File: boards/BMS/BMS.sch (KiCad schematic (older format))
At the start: 30 parts

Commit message: began isoSPI sheet, continued main sheet
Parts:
- added C?: C_0.1uF, Capacitors_SMD:C_0805, symbol C_0.1uF
- added D? (x5): LED_0805, LEDs:LED_0805, symbol LED_0805
- added Q? (x2): NMOS_GSD_30V, TO_SOT_Packages_SMD:SOT-23, symbol NMOS_GSD_30V
- added R? (x2): R_100k, Resistors_SMD:R_0805, symbol R_100k
- added R? (x2): R_10k, Resistors_SMD:R_0805, symbol R_10k
- added R? (x2): 649, symbol R
- added R? (x3): R_200, Resistors_SMD:R_0805, symbol R_200
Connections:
- net BSPD_Current_Sense: now also IC?.23 ((PCINT3/AMP0-)PB3)
- net GND: now also U?.3 (GND), C?.2, Q?.2 (S), Q?.2 (S), R?.1, R?.1, R?.1, R?.1, R?.2, R?.2, R?.2
- net LED1: now also IC?.17 ((PCINT12/ADC8/ACMPN3/AMP1-)PC4)
- net LED2: now also IC?.18 ((PCINT13/ADC9/ACMP3/AMP1+)PC5)
- net VCC: now also U?.5 (VCC), C?.1, R?.1, R?.1
- net Sense_Shutdown_N: now reaches IC?.14 ((PCINT22/ADC3/INT0/ACMPN2)PD6)
- net Sense_Shutdown_N: now also Q?.3 (D), R?.2
- net Sense_Shutdown_S: now reaches IC?.15 ((PCINT23/ACMP0)PD7)
- net Sense_Shutdown_S: now also Q?.3 (D), R?.2
- net Shutdown_Control: now reaches IC?.16 ((PCINT2/ADC5/INT1/ACMPN0)PB2)
- net CS_iso: now reaches IC?.24 ((PCINT4/AMP0+)PB4)
- net LED3: now reaches IC?.26 ((PCINT5/ADC6/INT2/ACMPN1/AMP2-)PB5)
- net LED3: now also D?.2 (A)
- net LED4: now reaches IC?.27 ((PCINT6/ADC7/PSCOUT1B)PB6)
- net LED4: now also D?.2 (A)
- net SCK_iso: now reaches IC?.28 ((PCINT7/ADC4/SCK/PSCOUT0B)PB7)
- net Fan_PWM: now reaches IC?.3 ((PCINT9/PSCIN1/OC1B/~SS_A~)PC1)
- net LED5: now reaches IC?.30 ((PCINT8/INT3/PSCOUT1A)PC0)
- net LED5: now also D?.2 (A)
- net MISO_iso: now reaches IC?.8 ((PCINT0/MISO/PSCOUT2A)PB0)
- net MOSI_iso: now reaches IC?.9 ((PCINT1/MOSI/PSCOUT2B)PB1)
- new net: D?.1 (K), R?.2 (x2)
- new net: D?.1 (K), R?.1 (x3)
- new net Shutdown_N: D?.2 (A), Q?.1 (G), R?.2
- new net Shutdown_S: D?.2 (A), Q?.1 (G), R?.2
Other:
- moved on the sheet: R?

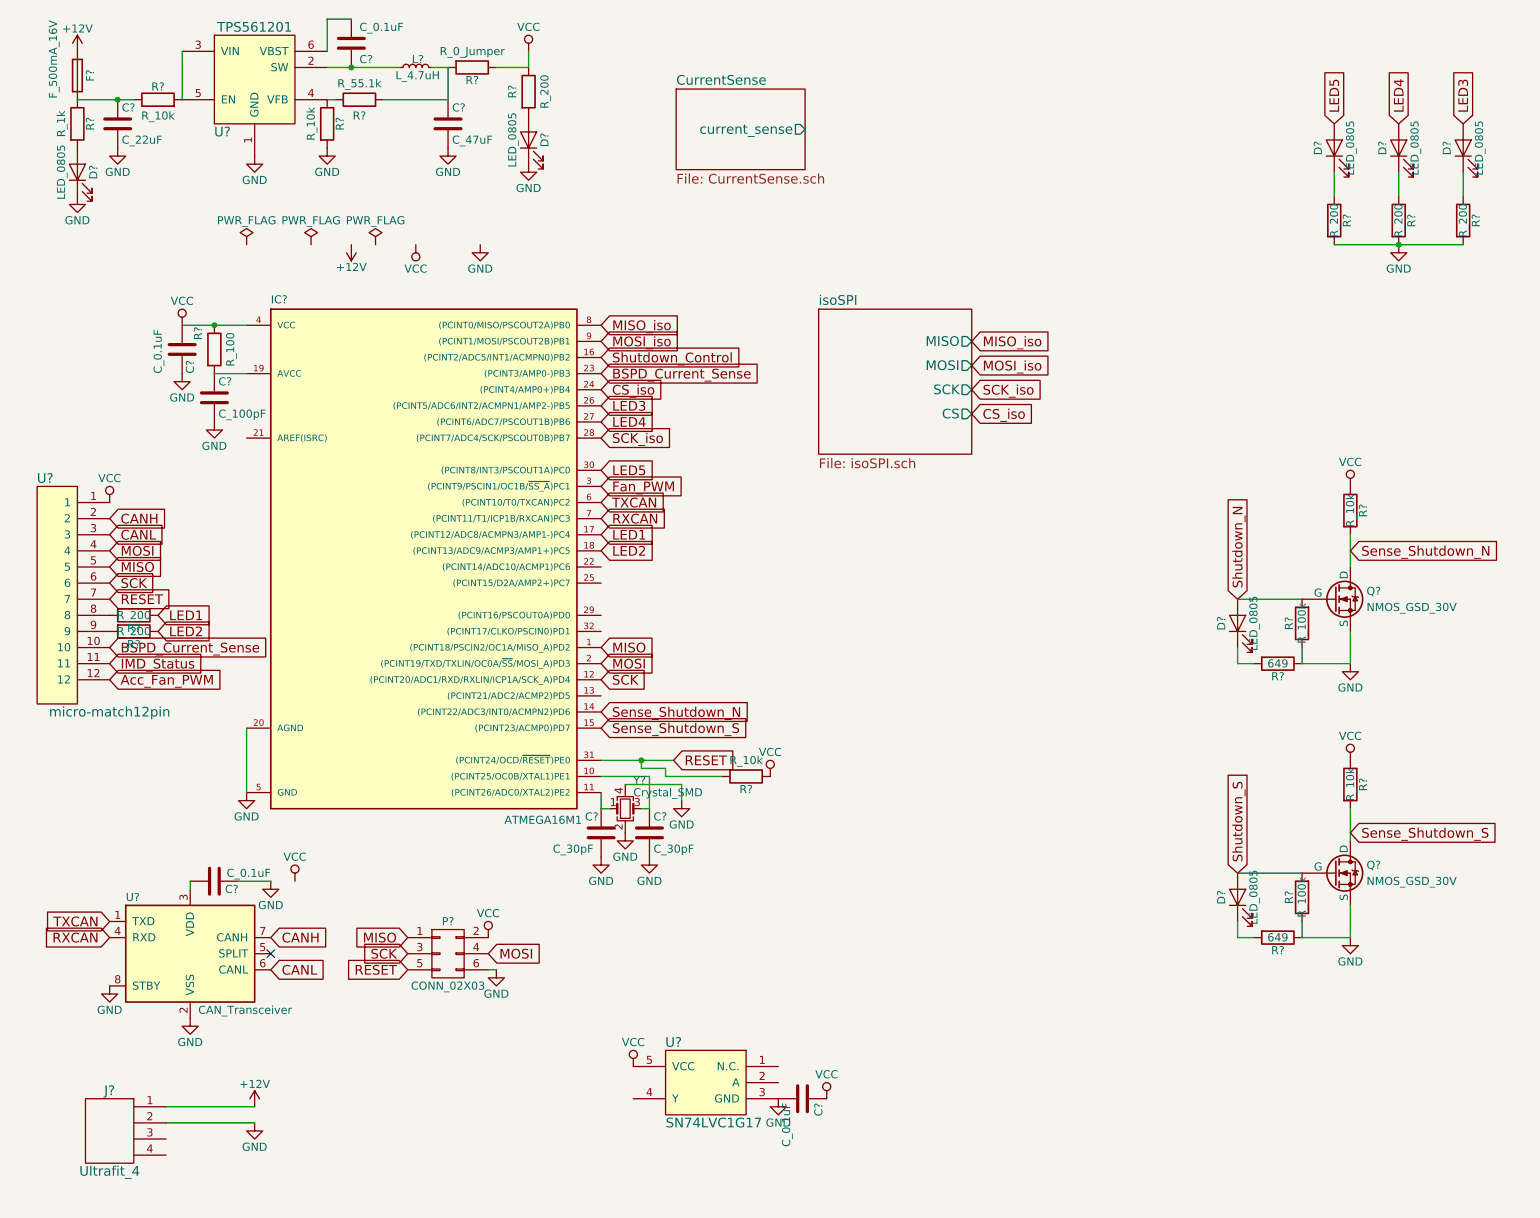
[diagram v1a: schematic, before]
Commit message: balance schematic for BMS slave
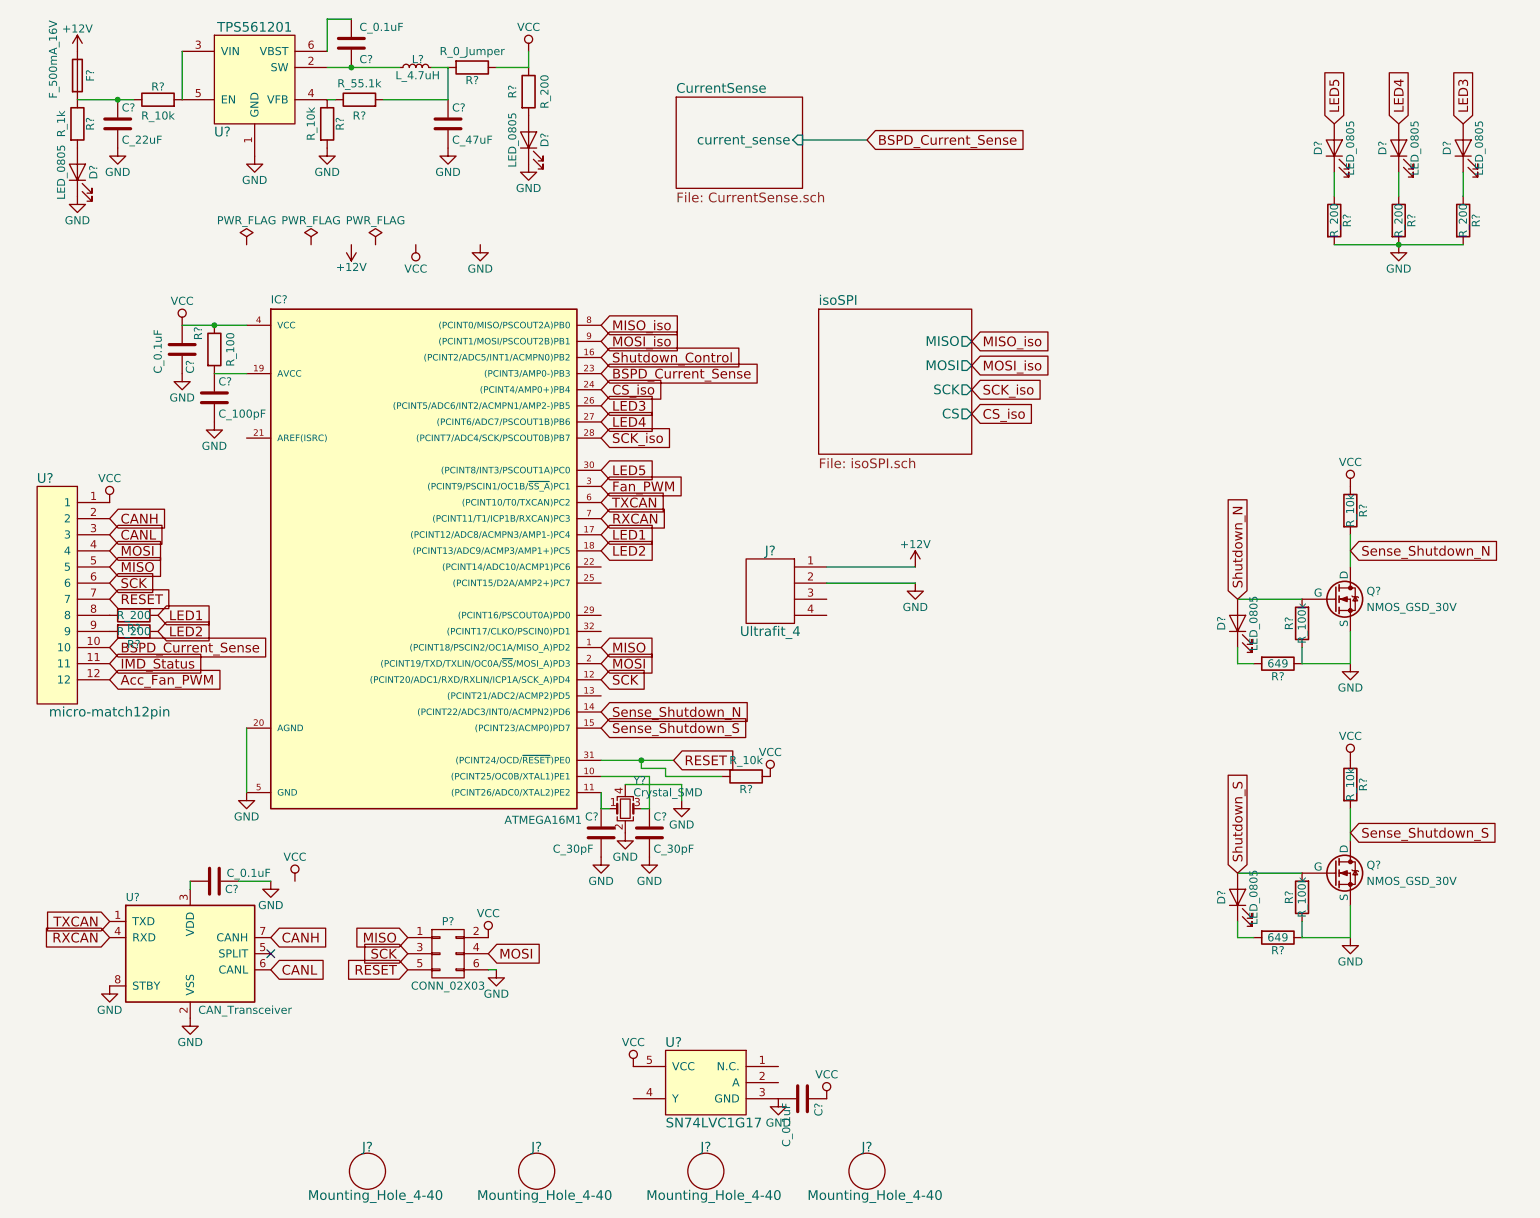
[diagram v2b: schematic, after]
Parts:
- added J? (x4): Mounting_Hole_4-40, footprints:Mounting_Hole_4-40, symbol Mounting_Hole_4-40
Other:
- moved on the sheet: J?
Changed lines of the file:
@@
 L Ultrafit_4 J?
 U 1 1 59E24F97
-P 1000 7600
-F 0 "J?" H 1000 7900 60  0000 C CNN
-F 1 "Ultrafit_4" H 1000 7400 60  0000 C CNN
-F 2 "footprints:Ultrafit_4" H 900 7850 60  0001 C CNN
-F 3 "http://www.literature.molex.com/SQLImages/kelmscott/Molex/PDF_Images/987651-1008.pdf" H 1000 7950 60  0001 C CNN
-F 4 "Digi-Key" H 1000 7600 60  0001 C CNN "MFN"
-F 5 "Value" H 1000 7600 60  0001 C CNN "Package"
-F 6 "WM11574-ND" H 1000 7600 60  0001 C CNN "MPN"
-F 7 "WM11564-ND" H 1400 8350 60  0001 C CNN "MPN2"
-F 8 "https://www.digikey.com/products/en?keywords=WM11574-ND" H 1500 8450 60  0001 C CNN "PurchasingLink"
-F 9 "https://www.digikey.com/product-detail/en/molex-llc/1722561004/WM11564-ND/5291228" H 1600 8550 60  0001 C CNN "PurchasingLink2"
-	1    1000 7600
+P 5100 4250
+F 0 "J?" H 5100 4550 60  0000 C CNN
+F 1 "Ultrafit_4" H 5100 4050 60  0000 C CNN
+F 2 "footprints:Ultrafit_4" H 5000 4500 60  0001 C CNN
+F 3 "http://www.literature.molex.com/SQLImages/kelmscott/Molex/PDF_Images/987651-1008.pdf" H 5100 4600 60  0001 C CNN
+F 4 "Digi-Key" H 5100 4250 60  0001 C CNN "MFN"
+F 5 "Value" H 5100 4250 60  0001 C CNN "Package"
+F 6 "WM11574-ND" H 5100 4250 60  0001 C CNN "MPN"
+F 7 "WM11564-ND" H 5500 5000 60  0001 C CNN "MPN2"
+F 8 "https://www.digikey.com/products/en?keywords=WM11574-ND" H 5600 5100 60  0001 C CNN "PurchasingLink"
+F 9 "https://www.digikey.com/product-detail/en/molex-llc/1722561004/WM11564-ND/5291228" H 5700 5200 60  0001 C CNN "PurchasingLink2"
+	1    5100 4250
 	1    0    0    -1
 $EndComp
@@
 L GND #PWR?
 U 1 1 59E25104
-P 1900 7500
-F 0 "#PWR?" H 1900 7250 50  0001 C CNN
-F 1 "GND" H 1900 7350 50  0000 C CNN
-F 2 "" H 1900 7500 50  0001 C CNN
-F 3 "" H 1900 7500 50  0001 C CNN
-	1    1900 7500
-	1    0    0    -1
-$EndComp
-Wire Wire Line
-	1350 7500 1900 7500
+P 6000 4150
+F 0 "#PWR?" H 6000 3900 50  0001 C CNN
+F 1 "GND" H 6000 4000 50  0000 C CNN
+F 2 "" H 6000 4150 50  0001 C CNN
+F 3 "" H 6000 4150 50  0001 C CNN
+	1    6000 4150
+	1    0    0    -1
+$EndComp
+Wire Wire Line
+	5450 4150 6000 4150
 $Comp
 L +12V #PWR?
 U 1 1 59E26B4D
-P 1900 7400
-F 0 "#PWR?" H 1900 7250 50  0001 C CNN
-F 1 "+12V" H 1900 7540 50  0000 C CNN
-F 2 "" H 1900 7400 50  0001 C CNN
-F 3 "" H 1900 7400 50  0001 C CNN
-	1    1900 7400
-	1    0    0    -1
-$EndComp
-Wire Wire Line
-	1900 7400 1350 7400
+P 6000 4050
+F 0 "#PWR?" H 6000 3900 50  0001 C CNN
+F 1 "+12V" H 6000 4190 50  0000 C CNN
+F 2 "" H 6000 4050 50  0001 C CNN
+F 3 "" H 6000 4050 50  0001 C CNN
+	1    6000 4050
+	1    0    0    -1
+$EndComp
+Wire Wire Line
+	6000 4050 5450 4050
 $Sheet
-S 4516 1084 800  500
+S 4516 1134 784  566
 U 59E289B4
 F0 "CurrentSense" 60
 F1 "CurrentSense.sch" 60
-F2 "current_sense" O R 5316 1334 60
+F2 "current_sense" I R 5300 1400 60
 $EndSheet
 $Comp
@@
 Wire Wire Line
 	4450 5350 4800 5350
+$Comp
+L Mounting_Hole_4-40 J?
+U 1 1 59E55DB0
+P 5700 7800
+F 0 "J?" H 5700 7950 60  0000 C CNN
+F 1 "Mounting_Hole_4-40" H 5750 7650 60  0000 C CNN
+F 2 "footprints:Mounting_Hole_4-40" H 5600 7850 60  0001 C CNN
+F 3 "" H 5700 7800 60  0001 C CNN
+F 4 "Value" H 5700 7800 60  0001 C CNN "MFN"
+F 5 "Value" H 5700 7800 60  0001 C CNN "MPN"
+F 6 "Value" H 5700 7800 60  0001 C CNN "Package"
+	1    5700 7800
+	1    0    0    -1
+$EndComp
+$Comp
+L Mounting_Hole_4-40 J?
+U 1 1 59E56289
+P 4700 7800
+F 0 "J?" H 4700 7950 60  0000 C CNN
+F 1 "Mounting_Hole_4-40" H 4750 7650 60  0000 C CNN
+F 2 "footprints:Mounting_Hole_4-40" H 4600 7850 60  0001 C CNN
+F 3 "" H 4700 7800 60  0001 C CNN
+F 4 "Value" H 4700 7800 60  0001 C CNN "MFN"
+F 5 "Value" H 4700 7800 60  0001 C CNN "MPN"
+F 6 "Value" H 4700 7800 60  0001 C CNN "Package"
+	1    4700 7800
+	1    0    0    -1
+$EndComp
+$Comp
+L Mounting_Hole_4-40 J?
+U 1 1 59E564F2
+P 3650 7800
+F 0 "J?" H 3650 7950 60  0000 C CNN
+F 1 "Mounting_Hole_4-40" H 3700 7650 60  0000 C CNN
+F 2 "footprints:Mounting_Hole_4-40" H 3550 7850 60  0001 C CNN
+F 3 "" H 3650 7800 60  0001 C CNN
+F 4 "Value" H 3650 7800 60  0001 C CNN "MFN"
+F 5 "Value" H 3650 7800 60  0001 C CNN "MPN"
+F 6 "Value" H 3650 7800 60  0001 C CNN "Package"
+	1    3650 7800
+	1    0    0    -1
+$EndComp
+$Comp
+L Mounting_Hole_4-40 J?
+U 1 1 59E565DE
+P 2600 7800
+F 0 "J?" H 2600 7950 60  0000 C CNN
+F 1 "Mounting_Hole_4-40" H 2650 7650 60  0000 C CNN
+F 2 "footprints:Mounting_Hole_4-40" H 2500 7850 60  0001 C CNN
+F 3 "" H 2600 7800 60  0001 C CNN
+F 4 "Value" H 2600 7800 60  0001 C CNN "MFN"
+F 5 "Value" H 2600 7800 60  0001 C CNN "MPN"
+F 6 "Value" H 2600 7800 60  0001 C CNN "Package"
+	1    2600 7800
+	1    0    0    -1
+$EndComp
+Text GLabel 5700 1400 2    60   Input ~ 0
+BSPD_Current_Sense
+Wire Wire Line
+	5300 1400 5700 1400
 $EndSCHEMATC
